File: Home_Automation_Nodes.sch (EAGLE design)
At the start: 19 parts

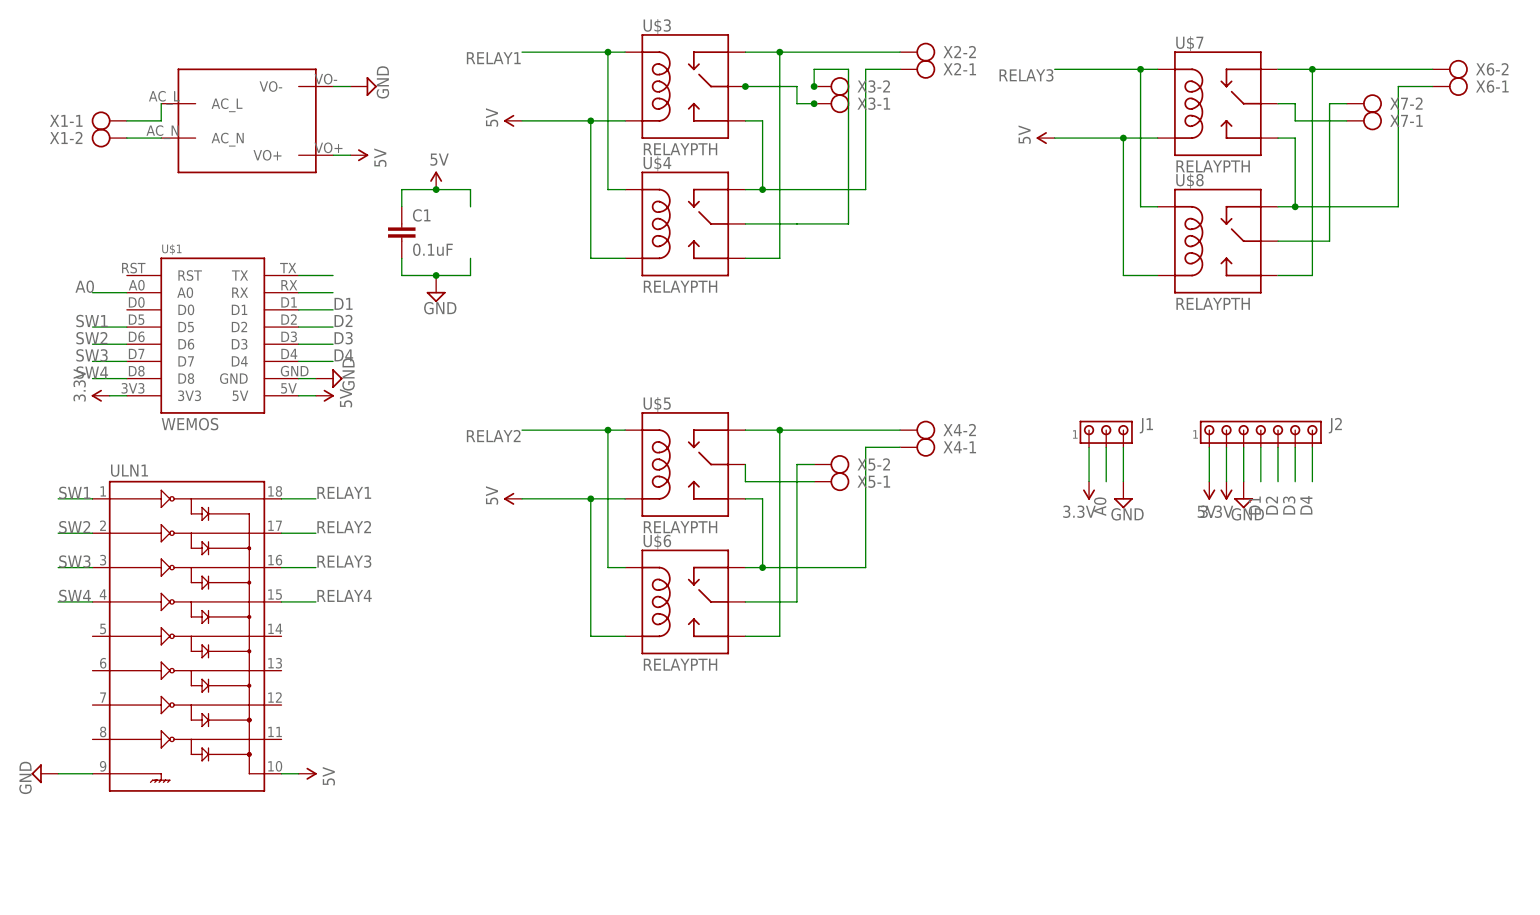
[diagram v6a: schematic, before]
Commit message: Changes: 1. WeMos D1 Mini Pads modified 2. Pins to ULN changed, to free the SPI channels 3. GND Plane added
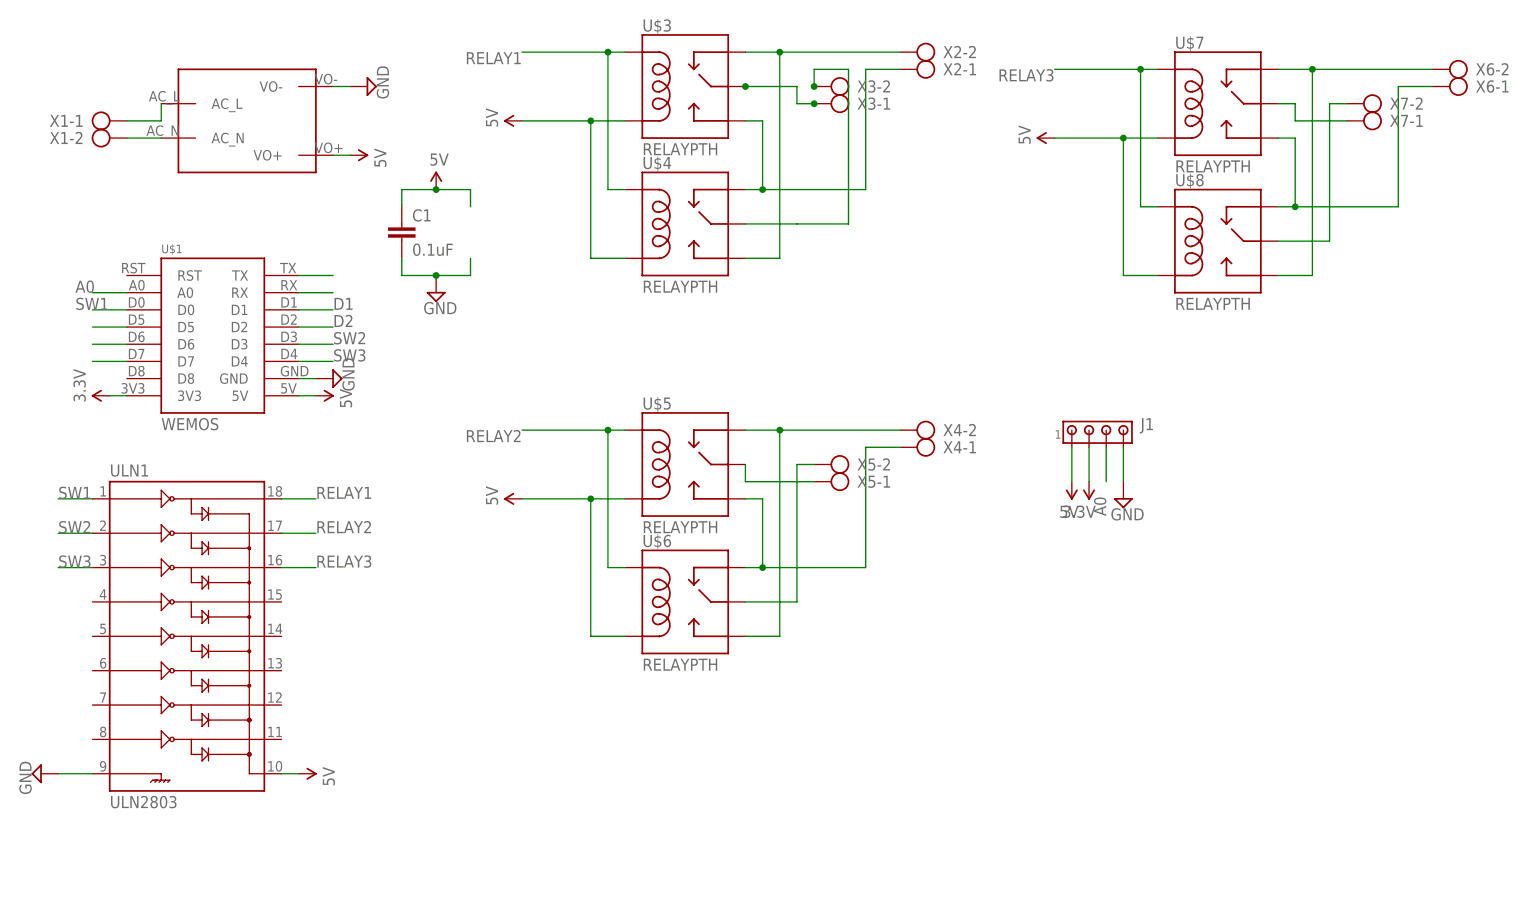
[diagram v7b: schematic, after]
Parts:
- removed J2: (no value), con-amp:MTA07-100
- J1: device con-amp:MTA03-100 -> con-amp:MTA04-100
- ULN1: value (none) -> ULN2803
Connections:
- removed net D3: J2.6, U$1.D3
- removed net D4: J2.7, U$1.D4
- removed net RELAY4: ULN1.15
- removed net SW4: U$1.D8, ULN1.4
- new net D5: U$1.D5
- new net D6: U$1.D6
- new net D7: U$1.D7
- net 3.3V: now also J1.2; no longer J1.1, J2.2
- net 5V: now also J1.1; no longer J2.1
- net A0: now also J1.3; no longer J1.2
- net D1: no longer J2.4
- net D2: no longer J2.5
- net GND: now also J1.4; no longer J1.3, J2.3
- net SW1: now also U$1.D0; no longer U$1.D5
- net SW2: now also U$1.D3; no longer U$1.D6
- net SW3: now also U$1.D4; no longer U$1.D7
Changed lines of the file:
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@@
 <part name="U$1" library="WeMos D1 Mini" deviceset="WEMOS" device=""/>
 <part name="U$2" library="captain-slow" deviceset="MAINS_CONVERTERS" device=""/>
-<part name="SUPPLY4" library="SparkFun-Aesthetics" deviceset="3.3V" device=""/>
 <part name="X1" library="con-ptr500" deviceset="AK300/2" device=""/>
-<part name="ULN1" library="SparkFun-PowerIC" deviceset="ULN2803" device="DIP"/>
+<part name="ULN1" library="SparkFun-PowerIC" deviceset="ULN2803" device="DIP" value="ULN2803"/>
 <part name="U$3" library="SRD-05VDC-SL-C" deviceset="RELAY" device="PTH"/>
 <part name="U$4" library="SRD-05VDC-SL-C" deviceset="RELAY" device="PTH"/>
@@
 <part name="SUPPLY8" library="SparkFun-Aesthetics" deviceset="5V" device=""/>
 <part name="SUPPLY9" library="supply2" deviceset="GND" device=""/>
-<part name="J1" library="con-amp" deviceset="MTA03-100" device=""/>
-<part name="J2" library="con-amp" deviceset="MTA07-100" device=""/>
 <part name="SUPPLY2" library="SparkFun-Aesthetics" deviceset="3.3V" device=""/>
-<part name="SUPPLY6" library="SparkFun-Aesthetics" deviceset="3.3V" device=""/>
-<part name="SUPPLY13" library="supply2" deviceset="GND" device=""/>
-<part name="SUPPLY15" library="SparkFun-Aesthetics" deviceset="5V" device=""/>
 <part name="C1" library="rcl" deviceset="C-EU" device="025-025X050" value="0.1uF"/>
 <part name="SUPPLY16" library="SparkFun-Aesthetics" deviceset="5V" device=""/>
@@
 <part name="SUPPLY11" library="SparkFun-Aesthetics" deviceset="5V" device=""/>
 <part name="SUPPLY12" library="SparkFun-Aesthetics" deviceset="5V" device=""/>
+<part name="SUPPLY4" library="SparkFun-Aesthetics" deviceset="3.3V" device=""/>
+<part name="J1" library="con-amp" deviceset="MTA04-100" device=""/>
+<part name="SUPPLY6" library="SparkFun-Aesthetics" deviceset="5V" device=""/>
 </parts>
 <sheets>
@@
 <instance part="U$1" gate="G$1" x="-30.48" y="81.28"/>
 <instance part="U$2" gate="G$1" x="-17.78" y="124.46"/>
-<instance part="SUPPLY4" gate="G$1" x="-38.1" y="83.82" rot="R90"/>
 <instance part="X1" gate="-1" x="-40.64" y="124.46"/>
 <instance part="X1" gate="-2" x="-40.64" y="121.92"/>
@@
 <instance part="SUPPLY8" gate="G$1" x="-10.16" y="27.94" rot="R270"/>
 <instance part="SUPPLY9" gate="GND" x="-48.26" y="27.94" rot="R270"/>
-<instance part="J1" gate="G$1" x="109.22" y="78.74"/>
-<instance part="J2" gate="G$1" x="132.08" y="78.74"/>
 <instance part="SUPPLY2" gate="G$1" x="106.68" y="71.12" rot="R180"/>
-<instance part="SUPPLY6" gate="G$1" x="127" y="71.12" rot="R180"/>
-<instance part="SUPPLY13" gate="GND" x="129.54" y="68.58"/>
-<instance part="SUPPLY15" gate="G$1" x="124.46" y="71.12" rot="R180"/>
 <instance part="C1" gate="G$1" x="5.08" y="109.22"/>
 <instance part="SUPPLY16" gate="G$1" x="10.16" y="114.3"/>
@@
 <instance part="SUPPLY11" gate="G$1" x="22.86" y="68.58" rot="R90"/>
 <instance part="SUPPLY12" gate="G$1" x="101.6" y="121.92" rot="R90"/>
+<instance part="SUPPLY4" gate="G$1" x="-38.1" y="83.82" rot="R90"/>
+<instance part="J1" gate="G$1" x="106.68" y="78.74"/>
+<instance part="SUPPLY6" gate="G$1" x="104.14" y="71.12" rot="R180"/>
 </instances>
 <busses>
@@
 <net name="3.3V" class="0">
 <segment>
-<pinref part="U$1" gate="G$1" pin="3V3"/>
-<pinref part="SUPPLY4" gate="G$1" pin="3.3V"/>
-<wire x1="-38.1" y1="83.82" x2="-35.56" y2="83.82" width="0.1524" layer="91"/>
-</segment>
-<segment>
-<pinref part="J1" gate="G$1" pin="1"/>
 <wire x1="106.68" y1="76.2" x2="106.68" y2="71.12" width="0.1524" layer="91"/>
 <pinref part="SUPPLY2" gate="G$1" pin="3.3V"/>
-</segment>
-<segment>
-<pinref part="J2" gate="G$1" pin="2"/>
-<wire x1="127" y1="76.2" x2="127" y2="71.12" width="0.1524" layer="91"/>
-<pinref part="SUPPLY6" gate="G$1" pin="3.3V"/>
+<pinref part="J1" gate="G$1" pin="2"/>
+</segment>
+<segment>
+<pinref part="U$1" gate="G$1" pin="3V3"/>
+<wire x1="-38.1" y1="83.82" x2="-35.56" y2="83.82" width="0.1524" layer="91"/>
+<pinref part="SUPPLY4" gate="G$1" pin="3.3V"/>
 </segment>
 </net>
@@
 </segment>
 <segment>
-<pinref part="U$1" gate="G$1" pin="D5"/>
-<wire x1="-35.56" y1="93.98" x2="-40.64" y2="93.98" width="0.1524" layer="91"/>
-<label x="-43.18" y="93.98" size="1.778" layer="95"/>
+<pinref part="U$1" gate="G$1" pin="D0"/>
+<wire x1="-35.56" y1="96.52" x2="-40.64" y2="96.52" width="0.1524" layer="91"/>
+<label x="-43.18" y="96.52" size="1.778" layer="95"/>
 </segment>
 </net>
@@
 </segment>
 <segment>
-<pinref part="U$1" gate="G$1" pin="D6"/>
-<wire x1="-35.56" y1="91.44" x2="-40.64" y2="91.44" width="0.1524" layer="91"/>
-<label x="-43.18" y="91.44" size="1.778" layer="95"/>
+<pinref part="U$1" gate="G$1" pin="D3"/>
+<wire x1="-10.16" y1="91.44" x2="-5.08" y2="91.44" width="0.1524" layer="91"/>
+<label x="-5.08" y="91.44" size="1.778" layer="95"/>
 </segment>
 </net>
@@
 </segment>
 <segment>
-<pinref part="U$1" gate="G$1" pin="D7"/>
-<wire x1="-35.56" y1="88.9" x2="-40.64" y2="88.9" width="0.1524" layer="91"/>
-<label x="-43.18" y="88.9" size="1.778" layer="95"/>
-</segment>
-</net>
-<net name="SW4" class="0">
-<segment>
-<pinref part="ULN1" gate="G$1" pin="4"/>
-<wire x1="-40.64" y1="53.34" x2="-45.72" y2="53.34" width="0.1524" layer="91"/>
-<label x="-45.72" y="53.34" size="1.778" layer="95"/>
-</segment>
-<segment>
-<pinref part="U$1" gate="G$1" pin="D8"/>
-<wire x1="-35.56" y1="86.36" x2="-40.64" y2="86.36" width="0.1524" layer="91"/>
-<label x="-43.18" y="86.36" size="1.778" layer="95"/>
+<pinref part="U$1" gate="G$1" pin="D4"/>
+<wire x1="-10.16" y1="88.9" x2="-5.08" y2="88.9" width="0.1524" layer="91"/>
+<label x="-5.08" y="88.9" size="1.778" layer="95"/>
 </segment>
 </net>
@@
 </segment>
 <segment>
-<pinref part="J2" gate="G$1" pin="1"/>
-<wire x1="124.46" y1="76.2" x2="124.46" y2="71.12" width="0.1524" layer="91"/>
-<pinref part="SUPPLY15" gate="G$1" pin="5V"/>
-</segment>
-<segment>
 <pinref part="C1" gate="G$1" pin="1"/>
 <wire x1="5.08" y1="111.76" x2="5.08" y2="114.3" width="0.1524" layer="91"/>
@@
 <pinref part="SUPPLY12" gate="G$1" pin="5V"/>
 </segment>
+<segment>
+<pinref part="J1" gate="G$1" pin="1"/>
+<wire x1="104.14" y1="76.2" x2="104.14" y2="71.12" width="0.1524" layer="91"/>
+<pinref part="SUPPLY6" gate="G$1" pin="5V"/>
+</segment>
 </net>
 <net name="GND" class="0">
@@
 <pinref part="SUPPLY5" gate="GND" pin="GND"/>
 <wire x1="-5.08" y1="129.54" x2="-2.54" y2="129.54" width="0.1524" layer="91"/>
-</segment>
-<segment>
-<pinref part="J2" gate="G$1" pin="3"/>
-<wire x1="129.54" y1="76.2" x2="129.54" y2="71.12" width="0.1524" layer="91"/>
-<pinref part="SUPPLY13" gate="GND" pin="GND"/>
 </segment>
 <segment>
@@
 </segment>
 <segment>
-<pinref part="J1" gate="G$1" pin="3"/>
 <wire x1="111.76" y1="76.2" x2="111.76" y2="71.12" width="0.1524" layer="91"/>
 <pinref part="SUPPLY14" gate="GND" pin="GND"/>
+<pinref part="J1" gate="G$1" pin="4"/>
 </segment>
 </net>
@@
 </segment>
 </net>
-<net name="RELAY4" class="0">
-<segment>
-<pinref part="ULN1" gate="G$1" pin="15"/>
-<wire x1="-12.7" y1="53.34" x2="-7.62" y2="53.34" width="0.1524" layer="91"/>
-<label x="-7.62" y="53.34" size="1.778" layer="95"/>
-</segment>
-</net>
 <net name="N$3" class="0">
 <segment>
@@
 </segment>
 <segment>
-<pinref part="J1" gate="G$1" pin="2"/>
 <wire x1="109.22" y1="76.2" x2="109.22" y2="71.12" width="0.1524" layer="91"/>
 <label x="109.22" y="66.04" size="1.778" layer="95" rot="R90"/>
+<pinref part="J1" gate="G$1" pin="3"/>
 </segment>
 </net>
@@
 <label x="-5.08" y="96.52" size="1.778" layer="95"/>
 </segment>
-<segment>
-<pinref part="J2" gate="G$1" pin="4"/>
-<wire x1="132.08" y1="76.2" x2="132.08" y2="71.12" width="0.1524" layer="91"/>
-<label x="132.08" y="66.04" size="1.778" layer="95" rot="R90"/>
-</segment>
 </net>
 <net name="D2" class="0">
@@
 <label x="-5.08" y="93.98" size="1.778" layer="95"/>
 </segment>
-<segment>
-<pinref part="J2" gate="G$1" pin="5"/>
-<wire x1="134.62" y1="76.2" x2="134.62" y2="71.12" width="0.1524" layer="91"/>
-<label x="134.62" y="66.04" size="1.778" layer="95" rot="R90"/>
-</segment>
-</net>
-<net name="D3" class="0">
-<segment>
-<pinref part="U$1" gate="G$1" pin="D3"/>
-<wire x1="-10.16" y1="91.44" x2="-5.08" y2="91.44" width="0.1524" layer="91"/>
-<label x="-5.08" y="91.44" size="1.778" layer="95"/>
-</segment>
-<segment>
-<pinref part="J2" gate="G$1" pin="6"/>
-<wire x1="137.16" y1="76.2" x2="137.16" y2="71.12" width="0.1524" layer="91"/>
-<label x="137.16" y="66.04" size="1.778" layer="95" rot="R90"/>
-</segment>
-</net>
-<net name="D4" class="0">
-<segment>
-<pinref part="U$1" gate="G$1" pin="D4"/>
-<wire x1="-10.16" y1="88.9" x2="-5.08" y2="88.9" width="0.1524" layer="91"/>
-<label x="-5.08" y="88.9" size="1.778" layer="95"/>
-</segment>
-<segment>
-<pinref part="J2" gate="G$1" pin="7"/>
-<wire x1="139.7" y1="76.2" x2="139.7" y2="71.12" width="0.1524" layer="91"/>
-<label x="139.7" y="66.04" size="1.778" layer="95" rot="R90"/>
-</segment>
 </net>
 <net name="N$16" class="0">
@@
 </segment>
 </net>
+<net name="D5" class="0">
+<segment>
+<pinref part="U$1" gate="G$1" pin="D5"/>
+<wire x1="-35.56" y1="93.98" x2="-40.64" y2="93.98" width="0.1524" layer="91"/>
+</segment>
+</net>
+<net name="D6" class="0">
+<segment>
+<pinref part="U$1" gate="G$1" pin="D6"/>
+<wire x1="-35.56" y1="91.44" x2="-40.64" y2="91.44" width="0.1524" layer="91"/>
+</segment>
+</net>
+<net name="D7" class="0">
+<segment>
+<pinref part="U$1" gate="G$1" pin="D7"/>
+<wire x1="-35.56" y1="88.9" x2="-40.64" y2="88.9" width="0.1524" layer="91"/>
+</segment>
+</net>
